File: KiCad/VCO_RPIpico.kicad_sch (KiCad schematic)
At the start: 51 parts, among them J1 AudioJack2, J2 Power Jack 5V, SW1 LFO1/2, SW2 Select LFO WaveForm, SW3 Fire4, SW4 Fire3, SW5 Fire2, SW6 Fire1, SW7 Shift2/Save, SW8 Shift1 / Select Bank, U1 PT2399 Modul

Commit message: KiCad
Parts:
- A1: footprint RPI_pico_Module:Raspberry_Pi_Pico_SMT_THT_noDebugPort -> MCU_RaspberryPi_and_Boards:RPi_Pico_SMD_TH
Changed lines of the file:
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@@
 			)
 		)
-		(property "Footprint" "RPI_pico_Module:Raspberry_Pi_Pico_SMT_THT_noDebugPort"
+		(property "Footprint" "MCU_RaspberryPi_and_Boards:RPi_Pico_SMD_TH"
 			(at 156.21 102.87 0)
 			(effects
@@
 					(unit 1)
 				)
-			)
-		)
-	)
-	(symbol
-		(lib_id "power:GND")
-		(at 50.8 163.83 0)
-		(unit 1)
-		(exclude_from_sim no)
-		(in_bom yes)
-		(on_board yes)
-		(dnp no)
-		(property "Reference" "#PWR025"
-			(at 50.8 170.18 0)
-			(effects
-				(font
-					(size 1.27 1.27)
-				)
-				(hide yes)
-			)
-		)
-		(property "Value" "GND"
-			(at 50.8 167.64 0)
-			(effects
-				(font
-					(size 1.27 1.27)
-				)
-			)
-		)
-		(property "Footprint" ""
-			(at 50.8 163.83 0)
-			(effects
-				(font
-					(size 1.27 1.27)
-				)
-				(hide yes)
-			)
-		)
-		(property "Datasheet" ""
-			(at 50.8 163.83 0)
-			(effects
-				(font
-					(size 1.27 1.27)
-				)
-				(hide yes)
-			)
-		)
-		(property "Description" ""
-			(at 50.8 163.83 0)
-			(effects
-				(font
-					(size 1.27 1.27)
-				)
-				(hide yes)
-			)
-		)
-		(pin "1"
-		)
-		(instances
-			(project "VCO_RPIpico"
-				(path "/0d855e99-162c-4989-8fe3-f98154ec6843"
-					(reference "#PWR025")
-					(unit 1)
-				)

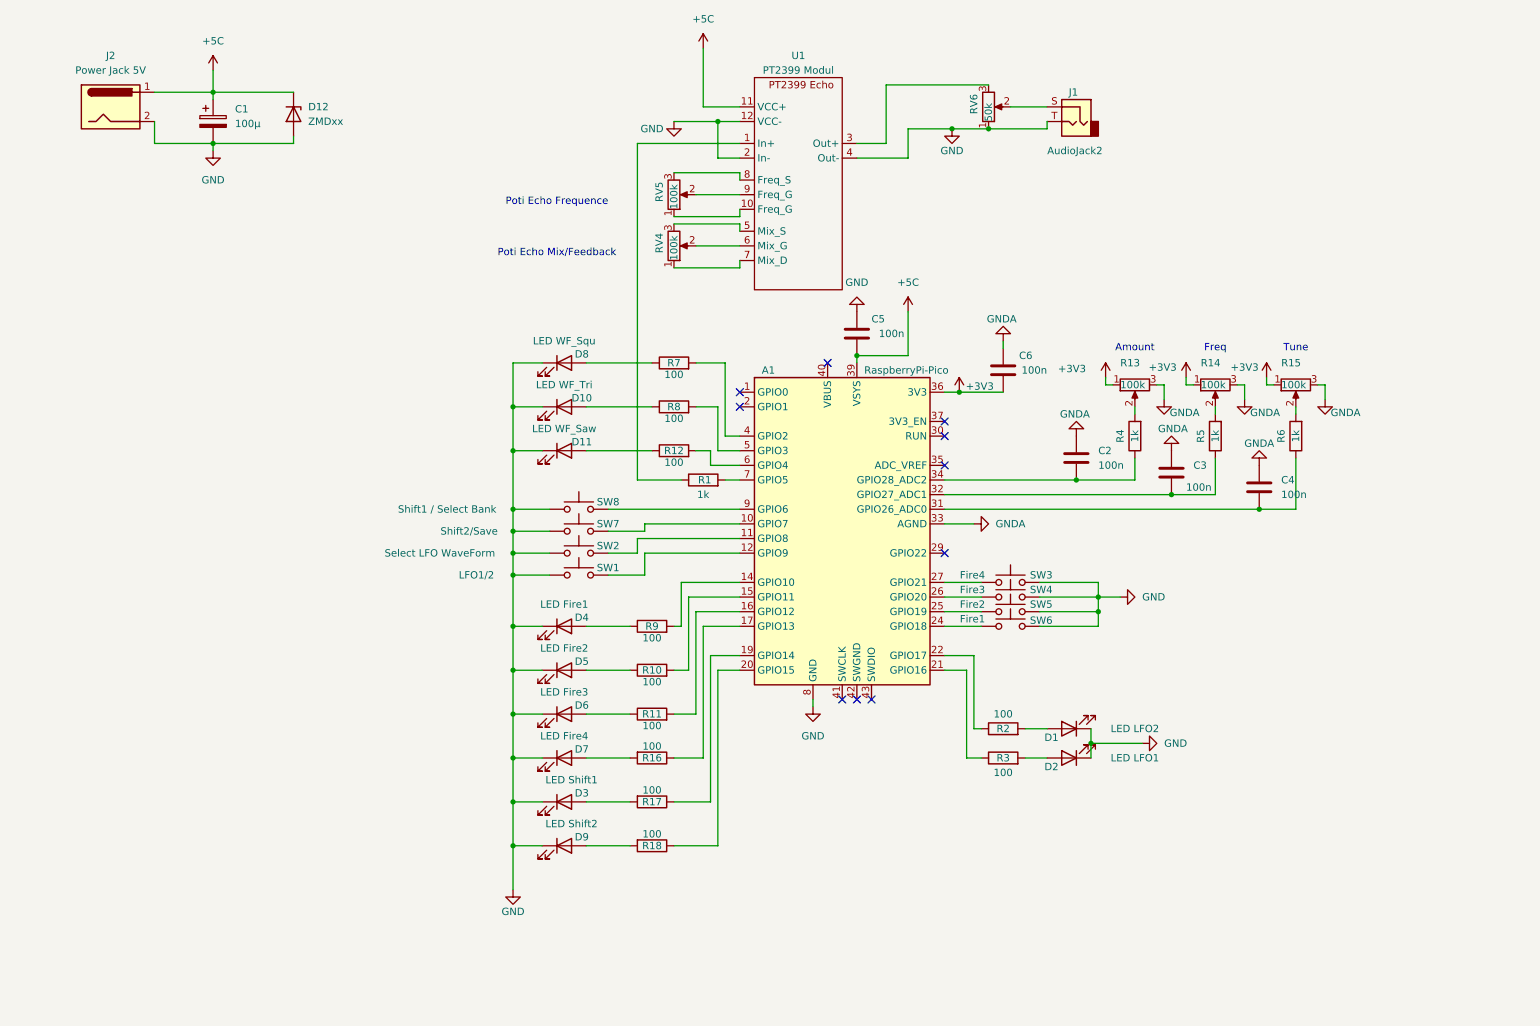
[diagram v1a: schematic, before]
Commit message: Echomodul diskret mit PT2399 implementiert
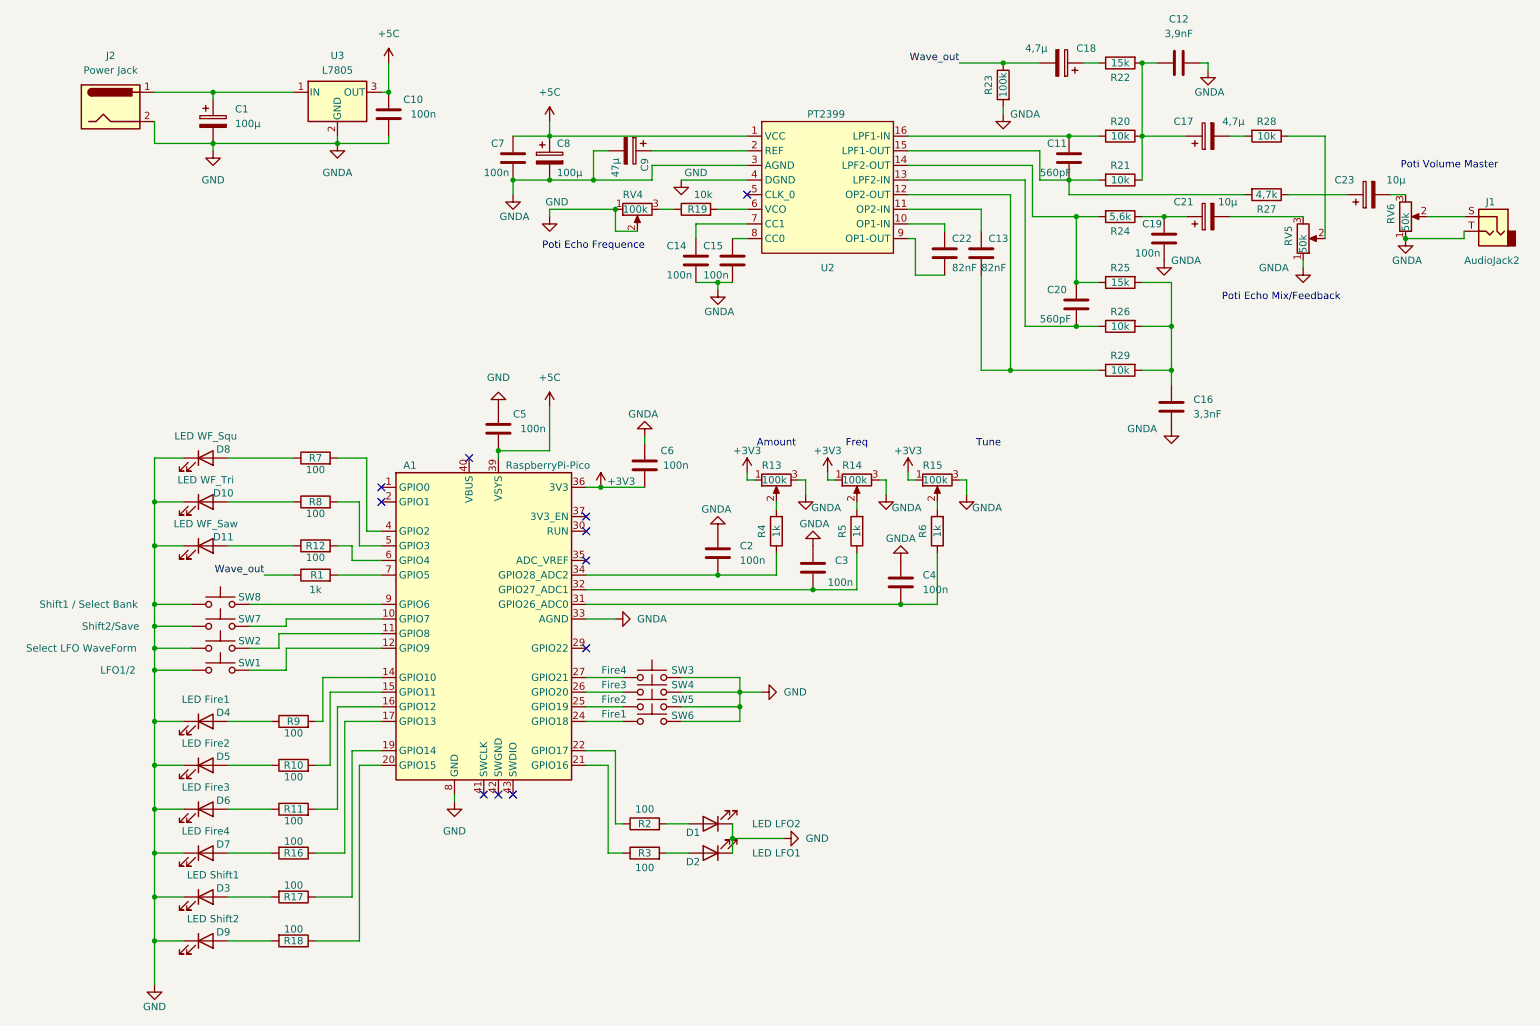
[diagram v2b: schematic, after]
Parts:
- removed D12: ZMDxx, Diode_SMD:D_MiniMELF, symbol Diode:ZMDxx
- removed U1: PT2399 Modul, PT2399_modul:PT2399_modul, symbol eigene_24:Echomodul_PT2399
- added C10, C14, C15, C19, C7: 100n, Capacitor_SMD:C_0805_2012Metric_Pad1.18x1.45mm_HandSolder, symbol Device:C
- added C11, C20: 560pF, Capacitor_SMD:C_0805_2012Metric_Pad1.18x1.45mm_HandSolder, symbol Device:C
- added C12: 3,9nF, Capacitor_SMD:C_0805_2012Metric_Pad1.18x1.45mm_HandSolder, symbol Device:C
- added C13, C22: 82nF, Capacitor_SMD:C_0805_2012Metric_Pad1.18x1.45mm_HandSolder, symbol Device:C
- added C16: 3,3nF, Capacitor_SMD:C_0805_2012Metric_Pad1.18x1.45mm_HandSolder, symbol Device:C
- added C17, C18: 4,7µ, symbol Device:C_Polarized
- added C21, C23: 10µ, symbol Device:C_Polarized
- added C8: 100µ, Capacitor_SMD:C_0805_2012Metric_Pad1.18x1.45mm_HandSolder, symbol Device:C_Polarized
- added C9: 47µ, symbol Device:C_Polarized
- added R19, R20, R21, R26, R28, R29: 10k, Resistor_SMD:R_1206_3216Metric, symbol Device:R
- added R22, R25: 15k, Resistor_SMD:R_1206_3216Metric, symbol Device:R
- added R23: 100k, Resistor_SMD:R_1206_3216Metric, symbol Device:R
- added R24: 5,6k, Resistor_SMD:R_1206_3216Metric, symbol Device:R
- added R27: 4,7k, Resistor_SMD:R_1206_3216Metric, symbol Device:R
- added U2: PT2399, Package_DIP:DIP-16_W7.62mm_Socket_LongPads, symbol eigene_24:PT2399
- added U3: L7805, Package_TO_SOT_SMD:TO-252-3_TabPin2, symbol Regulator_Linear:L7805
- C2, C3, C4, C5, C6: footprint Capacitor_SMD:C_1210_3225Metric -> Capacitor_SMD:C_0805_2012Metric_Pad1.18x1.45mm_HandSolder
- J2: value Power Jack 5V -> Power Jack
- RV5: value 100k -> 50k
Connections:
- net GNDA is gone; now on net GND: A1.33 (AGND), C2.1, C3.1, C4.1, C6.1, R13.3, R14.3, R15.3
- net +5C: now also C10.1, C7.1, C8.1, U2.1 (VCC), U3.3 (OUT); no longer C1.1, J2.1
- net GND: now also RV4.1, RV4.2, RV5.1, C10.2, C12.1, C14.2, C15.2, C16.2, C19.2, C7.2, C8.2, C9.2, R23.2, U2.3 (AGND), U2.4 (DGND), U3.2 (GND)
- net Wave_out: now reaches R1.1
- net Wave_out: now also C18.2, R23.1
- net at RV6.3: now also C23.2
- net at RV4.3: now also R19.1
- net at RV5.3: now also C21.2
- net at RV5.2: now also R28.1
- new net: C22.1, U2.10 (OP1-IN)
- new net: C22.2, U2.9 (OP1-OUT)
- new net: C20.1, R24.2, R25.1, U2.14 (LPF2-OUT)
- new net: C16.1, R25.2, R26.2, R29.2
- new net: C13.2, R29.1, U2.12 (OP2-OUT)
- new net: C12.2, C17.1, R20.1, R21.1, R22.2
- new net: C17.2, R28.2
- new net: C1.1, J2.1, U3.1 (IN)
- new net: C13.1, U2.11 (OP2-IN)
- new net: C20.2, R26.1, U2.13 (LPF2-IN)
- new net: C11.2, R21.2, R27.2, U2.15 (LPF1-OUT)
- new net: C11.1, R20.2, U2.16 (LPF1-IN)
- new net: C9.1, U2.2 (REF)
- new net: R19.2, U2.6 (VCO)
- new net: C14.1, U2.7 (CC1)
- new net: C15.1, U2.8 (CC0)
- new net: C23.1, R27.1
- new net: C18.1, R22.1
- new net: C19.1, C21.1, R24.1
- no-connect marks 10 -> 11
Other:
- note added: "Poti Volume Master"
- moved on the sheet: A1, C2, C3, C4, C5, C6, D1, D10, D11, D2, D3, D4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

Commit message: PCB Layout
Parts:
- C1: footprint Capacitor_SMD:CP_Elec_8x10.5 -> Capacitor_SMD:CP_Elec_6.3x5.8
- C17, C18: footprint (none) -> Capacitor_Tantalum_SMD:CP_EIA-2012-12_Kemet-R_Pad1.30x1.05mm_HandSolder
- C2, C3, C4, C5, C6, C7: footprint Capacitor_SMD:C_0805_2012Metric_Pad1.18x1.45mm_HandSolder -> Capacitor_SMD:C_1206_3216Metric
- C21, C23: footprint (none) -> Capacitor_SMD:CP_Elec_4x5.7
- C8: footprint Capacitor_SMD:C_0805_2012Metric_Pad1.18x1.45mm_HandSolder -> Capacitor_SMD:CP_Elec_6.3x5.8
- C9: footprint (none) -> Capacitor_SMD:CP_Elec_6.3x5.3
- D10: value LED WF_Tri -> LED_WF_Tri
- D11: value LED WF_Saw -> LED_WF_Saw
- D8: value LED WF_Squ -> LED_WF_Squ
- R10, R11, R12, R16, R17, R18, R2, R3, R7, R8, R9: value 100 -> 680
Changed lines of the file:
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@@
 	(wire
 		(pts
-			(xy 46.99 39.37) (xy 46.99 40.64)
+			(xy 46.99 39.37) (xy 46.99 41.91)
 		)
 		(stroke
@@
 	(wire
 		(pts
+			(xy 68.58 41.91) (xy 68.58 39.37)
+		)
+		(stroke
+			(width 0)
+			(type default)
+		)
+	)
+	(wire
+		(pts
 			(xy 213.36 63.5) (xy 213.36 71.12)
 		)
@@
 			)
 		)
-		(property "Value" "100"
+		(property "Value" "680"
 			(at 60.96 156.972 90)
 			(effects
@@
 	(symbol
 		(lib_id "power:GND")
-		(at 46.99 40.64 0)
+		(at 46.99 41.91 0)
 		(unit 1)
 		(exclude_from_sim no)
@@
 		(fields_autoplaced yes)
 		(property "Reference" "#PWR014"
-			(at 46.99 46.99 0)
+			(at 46.99 48.26 0)
 			(effects
 				(font
@@
 		)
 		(property "Value" "GND"
-			(at 46.99 45.72 0)
+			(at 46.99 46.99 0)
 			(effects
 				(font
@@
 		)
 		(property "Footprint" ""
-			(at 46.99 40.64 0)
+			(at 46.99 41.91 0)
 			(effects
 				(font
@@
 		)
 		(property "Datasheet" ""
-			(at 46.99 40.64 0)
+			(at 46.99 41.91 0)
 			(effects
 				(font
@@
 		)
 		(property "Description" ""
-			(at 46.99 40.64 0)
+			(at 46.99 41.91 0)
 			(effects
 				(font
@@
 			)
 		)
-		(property "Value" "100"
+		(property "Value" "680"
 			(at 64.77 103.632 90)
 			(effects
@@
 			)
 		)
-		(property "Value" "100"
+		(property "Value" "680"
 			(at 60.96 141.732 90)
 			(effects
@@
 			)
 		)
-		(property "Footprint" ""
+		(property "Footprint" "Capacitor_Tantalum_SMD:CP_EIA-2012-12_Kemet-R_Pad1.30x1.05mm_HandSolder"
 			(at 223.52 37.1348 0)
 			(effects
@@
 			)
 		)
-		(property "Footprint" ""
+		(property "Footprint" "Capacitor_SMD:CP_Elec_4x5.7"
 			(at 251.46 47.2948 0)
 			(effects
@@
 			)
 		)
-		(property "Footprint" ""
+		(property "Footprint" "Capacitor_Tantalum_SMD:CP_EIA-2012-12_Kemet-R_Pad1.30x1.05mm_HandSolder"
 			(at 190.5 24.4348 0)
 			(effects
@@
 			)
 		)
-		(property "Footprint" "Capacitor_SMD:C_0805_2012Metric_Pad1.18x1.45mm_HandSolder"
+		(property "Footprint" "Capacitor_SMD:C_1206_3216Metric"
 			(at 135.5852 114.3 0)
 			(effects
@@
 			)
 		)
-		(property "Footprint" "Capacitor_SMD:C_0805_2012Metric_Pad1.18x1.45mm_HandSolder"
+		(property "Footprint" "Capacitor_SMD:C_1206_3216Metric"
 			(at 167.3352 119.38 0)
 			(effects
@@
 			)
 		)
-		(property "Footprint" "Capacitor_SMD:C_0805_2012Metric_Pad1.18x1.45mm_HandSolder"
+		(property "Footprint" "Capacitor_SMD:C_1206_3216Metric"
 			(at 152.0952 116.84 0)
 			(effects
@@
 			)
 		)
-		(property "Footprint" "Capacitor_SMD:C_0805_2012Metric_Pad1.18x1.45mm_HandSolder"
+		(property "Footprint" "Capacitor_SMD:CP_Elec_6.3x5.8"
 			(at 106.3752 45.72 0)
 			(effects
@@
 			)
 		)
-		(property "Value" "100"
+		(property "Value" "680"
 			(at 64.77 96.012 90)
 			(effects
@@
 			)
 		)
-		(property "Value" "100"
+		(property "Value" "680"
 			(at 60.96 160.528 90)
 			(effects
@@
 			)
 		)
-		(property "Value" "LED WF_Squ"
+		(property "Value" "LED_WF_Squ"
 			(at 45.72 90.17 0)
 			(effects
@@
 	(symbol
 		(lib_id "power:GNDA")
-		(at 68.58 39.37 0)
+		(at 68.58 41.91 0)
 		(unit 1)
 		(exclude_from_sim no)
@@
 		(fields_autoplaced yes)
 		(property "Reference" "#PWR012"
-			(at 68.58 45.72 0)
+			(at 68.58 48.26 0)
 			(effects
 				(font
@@
 		)
 		(property "Value" "GNDA"
-			(at 68.58 44.45 0)
+			(at 68.58 46.99 0)
 			(effects
 				(font
@@
 		)
 		(property "Footprint" ""
-			(at 68.58 39.37 0)
+			(at 68.58 41.91 0)
 			(effects
 				(font
@@
 		)
 		(property "Datasheet" ""
-			(at 68.58 39.37 0)
+			(at 68.58 41.91 0)
 			(effects
 				(font
@@
 		)
 		(property "Description" "Power symbol creates a global label with name \"GNDA\" , analog ground"
-			(at 68.58 39.37 0)
+			(at 68.58 41.91 0)
 			(effects
 				(font
@@
 			)
 		)
-		(property "Value" "100"
+		(property "Value" "680"
 			(at 64.77 111.252 90)
 			(effects
@@
 			)
 		)
-		(property "Footprint" "Capacitor_SMD:C_0805_2012Metric_Pad1.18x1.45mm_HandSolder"
+		(property "Footprint" "Capacitor_SMD:C_1206_3216Metric"
 			(at 97.4852 92.71 0)
 			(effects
@@
 			)
 		)
-		(property "Value" "LED WF_Tri"
+		(property "Value" "LED_WF_Tri"
 			(at 45.72 97.79 0)
 			(effects
@@
 			)
 		)
-		(property "Value" "100"
+		(property "Value" "680"
 			(at 60.96 175.768 90)
 			(effects
@@
 			)
 		)
-		(property "Value" "LED WF_Saw"
+		(property "Value" "LED_WF_Saw"
 			(at 45.72 105.41 0)
 			(effects
@@
 			)
 		)
-		(property "Footprint" "Capacitor_SMD:C_0805_2012Metric_Pad1.18x1.45mm_HandSolder"
+		(property "Footprint" "Capacitor_SMD:C_1206_3216Metric"
 			(at 120.9548 99.06 0)
 			(effects
@@
 			)
 		)
-		(property "Value" "100"
+		(property "Value" "680"
 			(at 121.92 165.1 90)
 			(effects
@@
 			)
 		)
-		(property "Value" "100"
+		(property "Value" "680"
 			(at 60.96 149.352 90)
 			(effects
@@
 			)
 		)
-		(property "Value" "100"
+		(property "Value" "680"
 			(at 60.96 168.148 90)
 			(effects
@@
 			)
 		)
-		(property "Value" "100"
+		(property "Value" "680"
 			(at 121.92 154.94 90)
 			(effects
@@
 			)
 		)
-		(property "Footprint" "Capacitor_SMD:CP_Elec_8x10.5"
+		(property "Footprint" "Capacitor_SMD:CP_Elec_6.3x5.8"
 			(at 47.9552 39.37 0)
 			(effects
@@
 			)
 		)
-		(property "Footprint" "Capacitor_SMD:C_0805_2012Metric_Pad1.18x1.45mm_HandSolder"
+		(property "Footprint" "Capacitor_SMD:C_1206_3216Metric"
 			(at 100.0252 45.72 0)
 			(effects
@@
 			)
 		)
-		(property "Footprint" ""
+		(property "Footprint" "Capacitor_SMD:CP_Elec_6.3x5.3"
 			(at 115.57 41.6052 0)
 			(effects
@@
 			)
 		)
-		(property "Footprint" ""
+		(property "Footprint" "Capacitor_SMD:CP_Elec_4x5.7"
 			(at 223.52 51.1048 0)
 			(effects
